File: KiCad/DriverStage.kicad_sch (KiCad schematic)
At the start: 3 parts, among them U2 DRV8323HRTAT

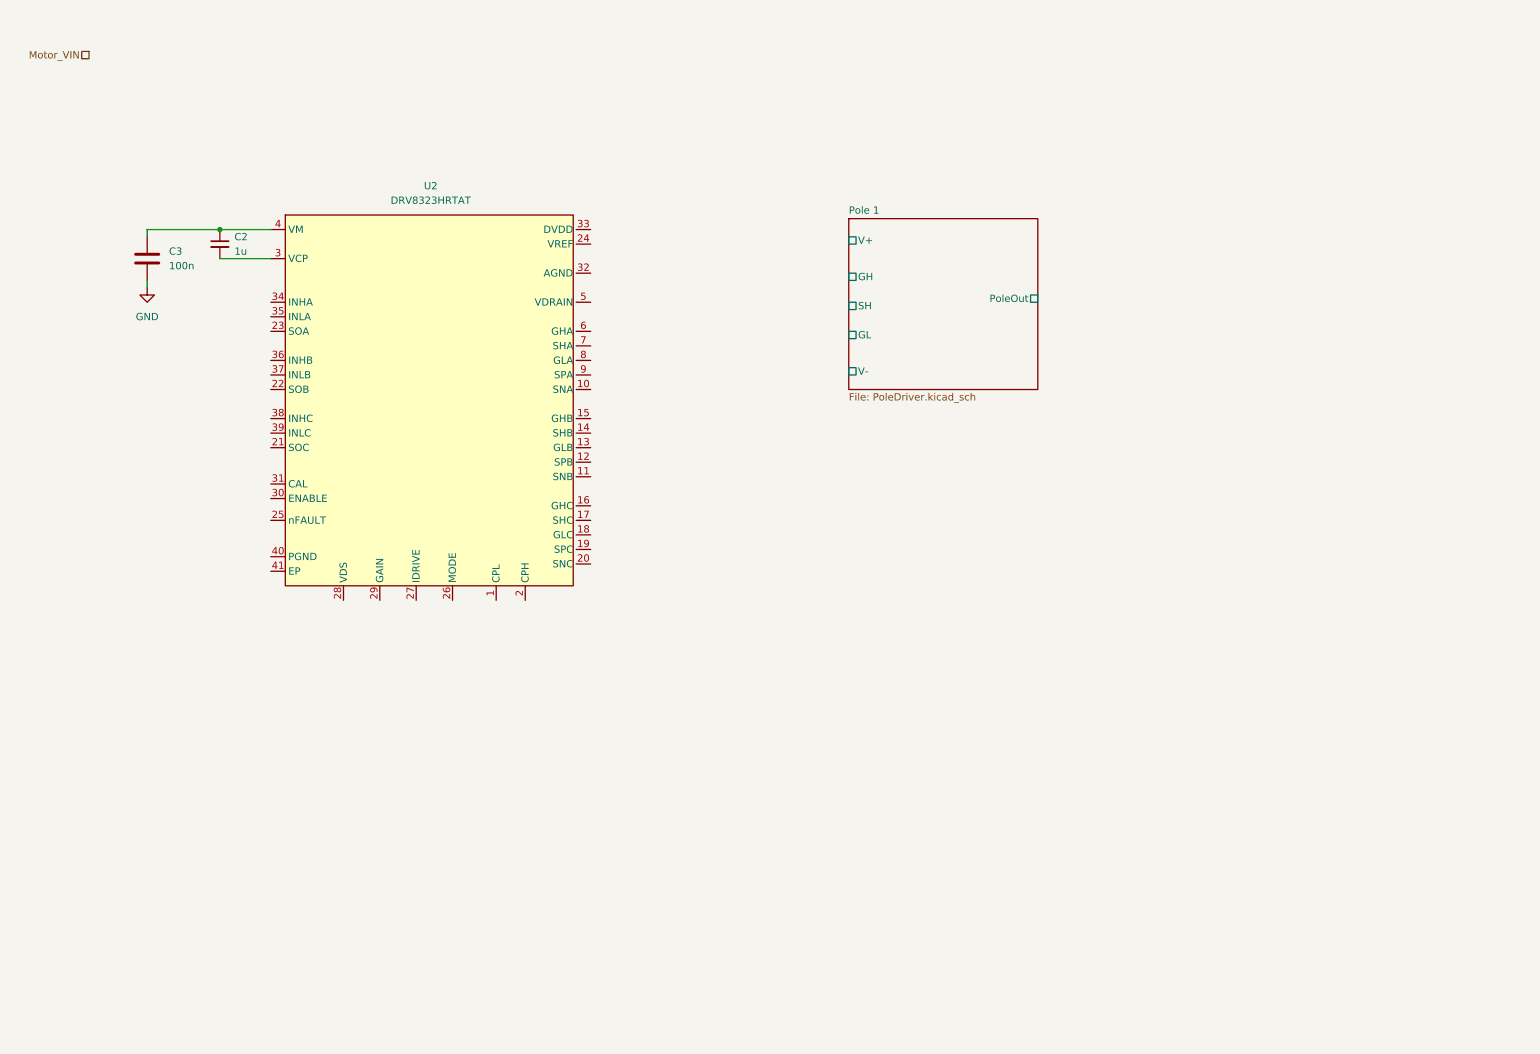
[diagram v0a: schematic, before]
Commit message: High current drive routing
Add TDSON-8 3D models and footprint (.step, .wrl, .kicad_mod) and update easyeda2kicad library; modify KiCad schematic sheets (DriverStage.kicad_sch, PoleDriver.kicad_sch, simpleFOC Dual Motor Controller.kicad_sch) to reposition symbols/wires, add connector symbol instances, and refresh UUIDs and component references (e.g. C2/C3/U2 -> C202/C201/U201). Also update PCB and project files to reflect schematic changes so footprints and global labels stay in sync.
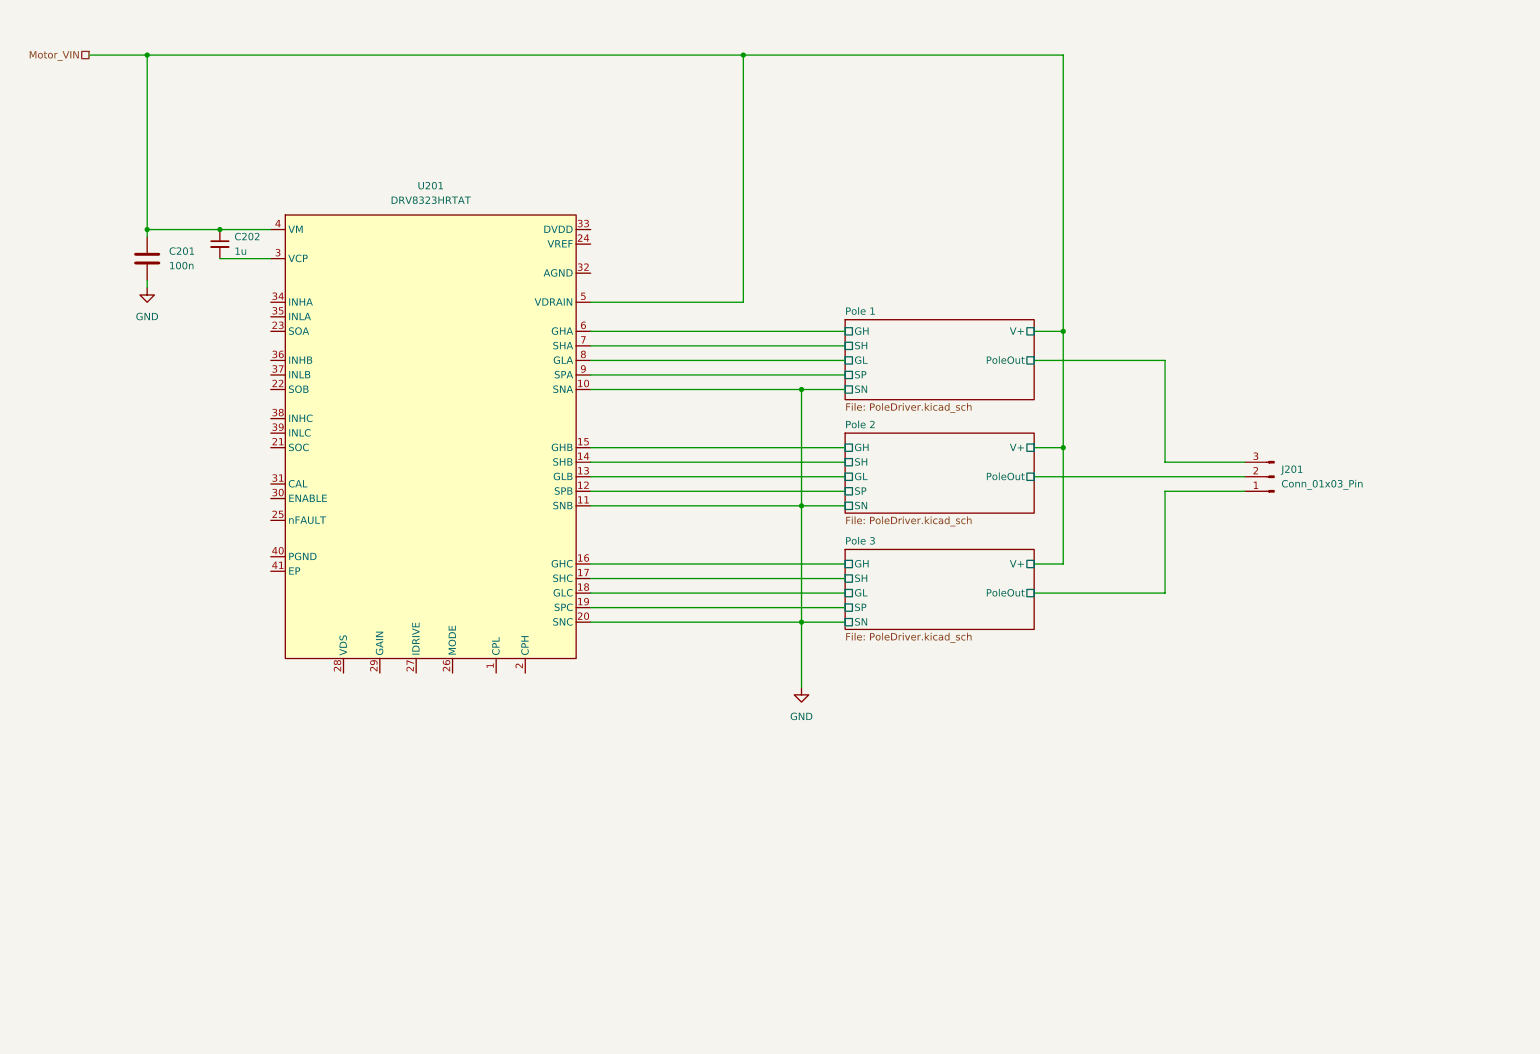
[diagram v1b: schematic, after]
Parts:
- added J201: Conn_01x03_Pin, symbol Connector:Conn_01x03_Pin
- renumbered C3 to C201, C2 to C202, U2 to U201
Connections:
- net GND: now also U201.10 (SNA), U201.11 (SNB), U201.20 (SNC)
- net Motor_VIN: now also C201.1, C202.1, U201.4 (VM), U201.5 (VDRAIN)
- net Pole 1/GH: now also U201.6 (GHA)
- net Pole 1/GL: now also U201.8 (GLA)
- net Pole 1/PoleOut: now also J201.3 (Pin_3)
- net Pole 1/SH: now also U201.7 (SHA)
- net Pole 2/SP: now reaches U201.12 (SPB)
- net Pole 2/GL: now reaches U201.13 (GLB)
- net Pole 2/SH: now reaches U201.14 (SHB)
- net Pole 2/GH: now reaches U201.15 (GHB)
- net Pole 3/GH: now reaches U201.16 (GHC)
- net Pole 3/SH: now reaches U201.17 (SHC)
- net Pole 3/GL: now reaches U201.18 (GLC)
- net Pole 3/SP: now reaches U201.19 (SPC)
- net Pole 1/SP: now reaches U201.9 (SPA)
- new net Pole 2/PoleOut: J201.2 (Pin_2)
- new net Pole 3/PoleOut: J201.1 (Pin_1)
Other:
- added sheet Pole 2 (PoleDriver.kicad_sch)
- added sheet Pole 3 (PoleDriver.kicad_sch)
- sheet Pole 1 ports: added SN, SP; removed V-
- moved on the sheet: U201

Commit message: Finished wiring motor drive circuitry
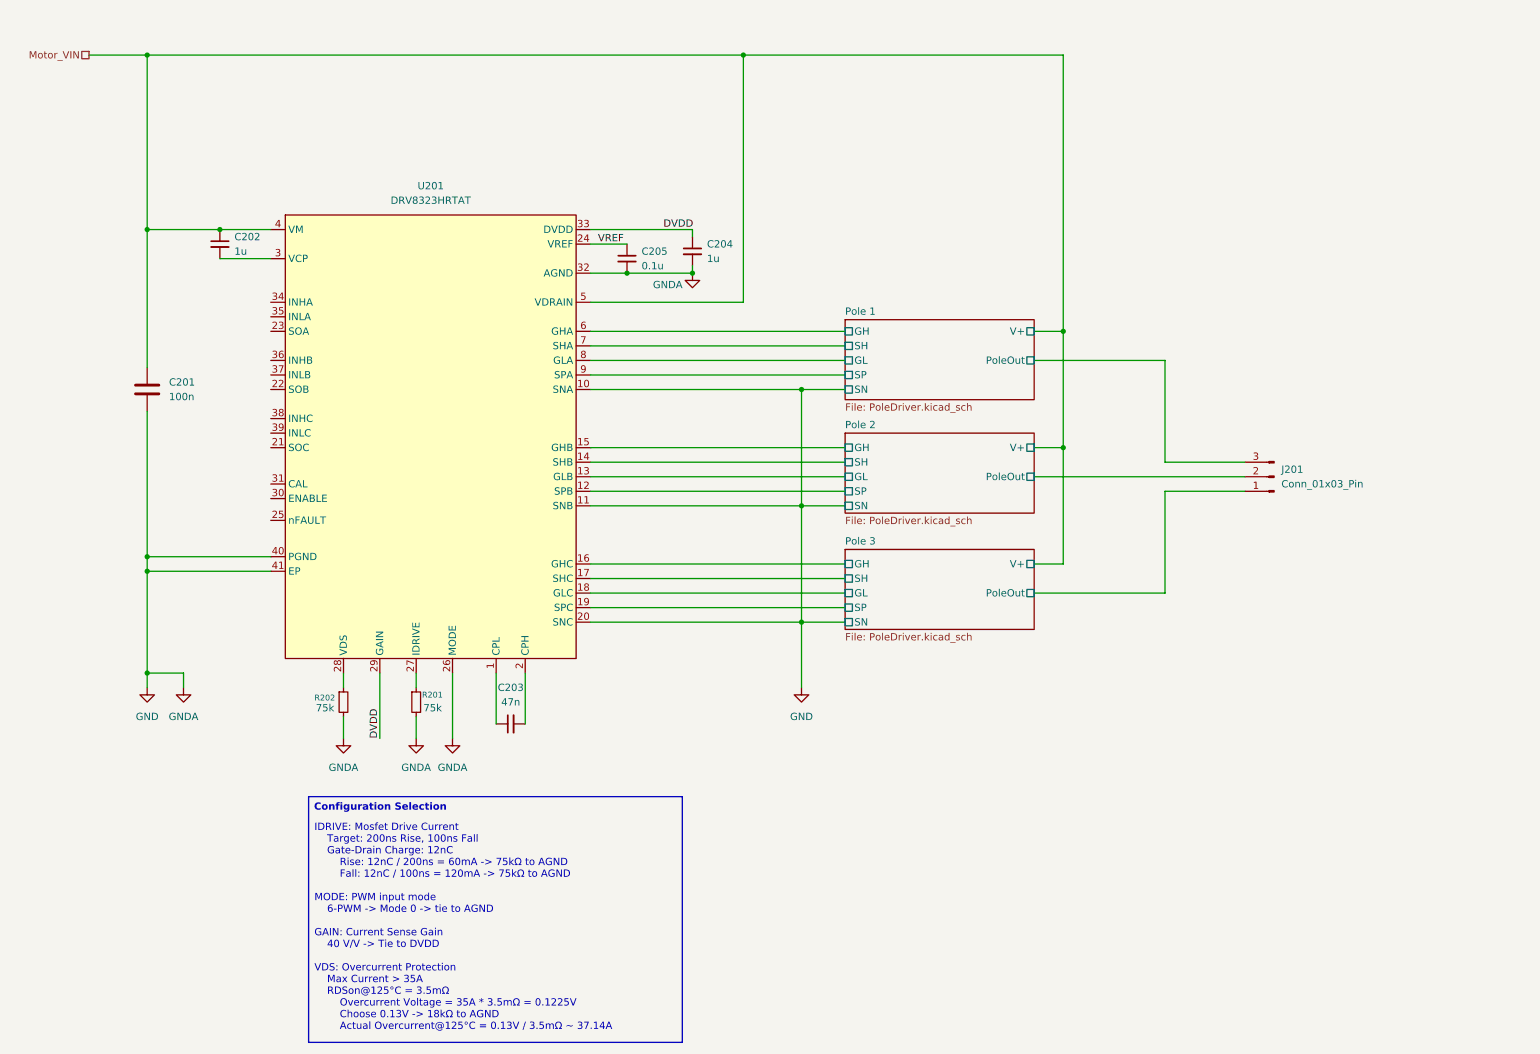
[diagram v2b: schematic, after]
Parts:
- added C203: 47n, Capacitor_SMD:C_0603_1608Metric, symbol Device:C_Small
- added C204: 1u, Capacitor_SMD:C_0402_1005Metric, symbol Device:C_Small
- added C205: 0.1u, Capacitor_SMD:C_0402_1005Metric, symbol Device:C_Small
- added R201, R202: 75k, symbol Device:R_Small
- C201: footprint (none) -> Capacitor_SMD:C_0805_2012Metric
- C202: footprint (none) -> Capacitor_SMD:C_0603_1608Metric
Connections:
- net GND: now also U201.26 (MODE), U201.32 (AGND), U201.40 (PGND), U201.41 (EP), C204.2, C205.2, R201.2, R202.2
- net at U201.1 (CPL): now also C203.1
- net at U201.2 (CPH): now also C203.2
- net VREF: now reaches U201.24 (VREF)
- net VREF: now also C205.1
- net at U201.27 (IDRIVE): now also R201.1
- net at U201.28 (VDS): now also R202.1
- net DVDD: now reaches U201.29 (GAIN)
- net DVDD: now also U201.33 (DVDD), C204.1
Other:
- note added: "IDRIVE: Mosfet Drive Current Target: 200ns Rise, 100ns Fall Gate-Drain Charge: 12nC Rise: 12nC / 200ns = 60mA -> 75kΩ to AGND Fall: 12nC / 100ns = 120mA -> 75kΩ to AGND MODE: PWM input mode 6-PWM -> Mode 0 -> tie to AGND GAIN: Current Sense Gain 40 V/V -> Tie to DVDD VDS: Overcurrent Protection Max Current > 35A RDSon@125°C = 3.5mΩ Overcurrent Voltage = 35A * 3.5mΩ = 0.1225V Choose 0.13V -> 18kΩ 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"
- moved on the sheet: C201

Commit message: started adding supporting components
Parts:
- R201, R202: footprint (none) -> Resistor_SMD:R_0402_1005Metric
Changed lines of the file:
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@@
 			)
 		)
-		(property "Footprint" ""
+		(property "Footprint" "Resistor_SMD:R_0402_1005Metric"
 			(at 85.09 137.16 0)
 			(hide yes)
@@
 			)
 		)
-		(property "Footprint" ""
+		(property "Footprint" "Resistor_SMD:R_0402_1005Metric"
 			(at 72.39 137.16 0)
 			(hide yes)

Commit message: rewired the board with smaller mosfets
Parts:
- removed J201: Conn_01x03_Pin, symbol Connector:Conn_01x03_Pin
- added CN201: MR60-F, easyeda2kicad:CONN-TH_3P-P5.50_MR60-F, symbol easyeda2kicad:MR60-F
- added NT201, NT202, NT203: NetTie_2, CustomNetTie:NetTie0.127mm, symbol Device:NetTie_2
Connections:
- net GND: now also NT201.2, NT202.2, NT203.2; no longer U201.10 (SNA), U201.11 (SNB), U201.20 (SNC)
- net Pole 1/PoleOut: now also CN201.1
- net Pole 2/PoleOut: now also CN201.2
- net Pole 3/PoleOut: now also CN201.3
- new net: NT201.1, U201.10 (SNA)
- new net: NT203.1, U201.20 (SNC)
- new net: NT202.1, U201.11 (SNB)

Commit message: start adding control pins
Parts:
- added R203, R204, R205, R206, R207, R208, R209, R210, R211: 100k, Resistor_SMD:R_0402_1005Metric, symbol Device:R_Small
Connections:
- net GND: now also R203.2, R204.2, R205.2, R206.2, R207.2, R208.2, R209.2, R210.2
- net SOC: now reaches U201.21 (SOC)
- net SOB: now reaches U201.22 (SOB)
- net SOA: now reaches U201.23 (SOA)
- net FAULT: now reaches U201.25 (nFAULT)
- net EN: now reaches U201.30 (ENABLE)
- net EN: now also R209.1
- net CAL: now reaches U201.31 (CAL)
- net CAL: now also R210.1
- net INHA: now reaches U201.34 (INHA)
- net INHA: now also R203.1
- net INLA: now reaches U201.35 (INLA)
- net INLA: now also R204.1
- net INHB: now reaches U201.36 (INHB)
- net INHB: now also R205.1
- net INLB: now reaches U201.37 (INLB)
- net INLB: now also R206.1
- net INHC: now reaches U201.38 (INHC)
- net INHC: now also R207.1
- net INLC: now reaches U201.39 (INLC)
- net INLC: now also R208.1
- new net 3.3V: R211.2
- new net ~{FAULT}: R211.1

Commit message: condensed
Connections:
- net FAULT is gone; now on net ~{FAULT}: U201.25 (nFAULT)
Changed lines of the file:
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@@
-		)
-	)
-	(hierarchical_label "FAULT"
-		(shape output)
-		(at 54.61 105.41 180)
-		(effects
-			(font
-				(size 1.27 1.27)
-			)
-			(justify right)
 		)
 	)
@@
 		(effects
 			(font
+				(size 1.27 1.27)
+			)
+			(justify right)
+		)
+	)
+	(hierarchical_label "~{FAULT}"
+		(shape output)
+		(at 54.61 105.41 180)
+		(effects
+			(font
